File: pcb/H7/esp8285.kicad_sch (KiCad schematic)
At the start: 12 parts, among them U26 ESP8266EX

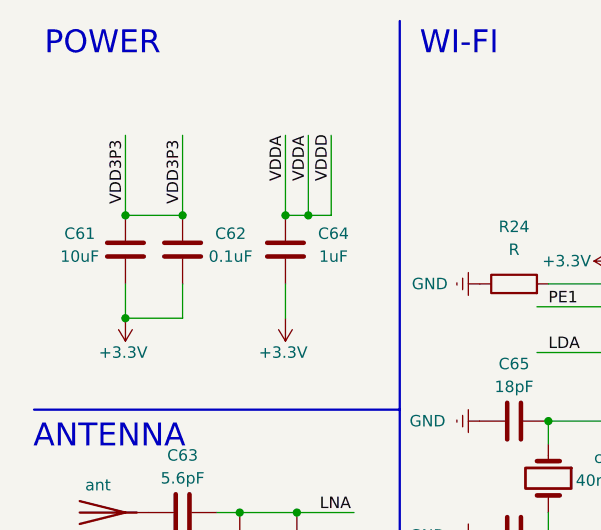
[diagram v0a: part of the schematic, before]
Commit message: schematic source updated
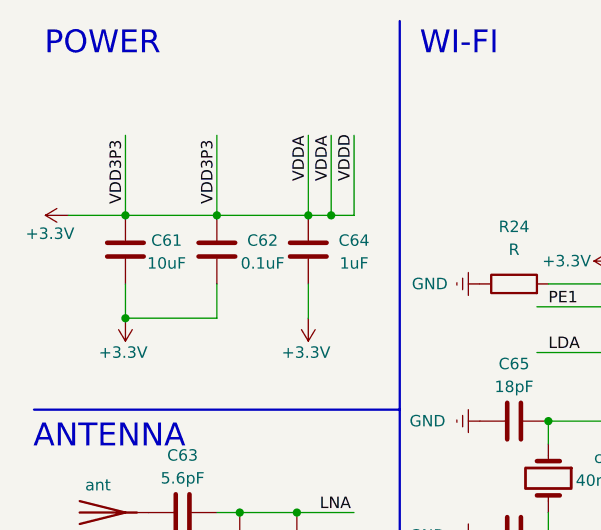
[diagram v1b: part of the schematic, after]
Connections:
- net VDD3P3 is gone; now on net +3.3V: C61.1, C62.2, U26.3 (VDD3P3), U26.4 (VDD3P3)
- net VDDA is gone; now on net +3.3V: C64.2, U26.1 (VDDA), U26.29 (VDDD), U26.30 (VDDA)
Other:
- moved on the sheet: C62, C64

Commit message: schematic fix
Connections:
- net +3.3V: no longer C61.2, C62.1, C64.1
- net GND: now also C61.2, C62.1, C64.1
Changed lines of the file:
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@@
+	)
+	(junction
+		(at 102.87 93.98)
+		(diameter 0)
+		(color 0 0 0 0)
 	)
 	(junction
@@
 	(junction
 		(at 115.57 115.57)
-		(diameter 0)
-		(color 0 0 0 0)
-	)
-	(junction
-		(at 102.87 93.98)
 		(diameter 0)
 		(color 0 0 0 0)
@@
 	(symbol
 		(lib_id "power:GNDREF")
+		(at 123.19 93.98 0)
+		(unit 1)
+		(exclude_from_sim no)
+		(in_bom yes)
+		(on_board yes)
+		(dnp no)
+		(property "Reference" "#PWR05"
+			(at 123.19 100.33 0)
+			(effects
+				(font
+					(size 1.27 1.27)
+				)
+				(hide yes)
+			)
+		)
+		(property "Value" "GND"
+			(at 124.968 98.044 0)
+			(effects
+				(font
+					(size 1.27 1.27)
+				)
+				(justify right)
+			)
+		)
+		(property "Footprint" ""
+			(at 123.19 93.98 0)
+			(effects
+				(font
+					(size 1.27 1.27)
+				)
+				(hide yes)
+			)
+		)
+		(property "Datasheet" ""
+			(at 123.19 93.98 0)
+			(effects
+				(font
+					(size 1.27 1.27)
+				)
+				(hide yes)
+			)
+		)
+		(property "Description" "Power symbol creates a global label with name \"GNDREF\" , reference supply ground"
+			(at 123.19 93.98 0)
+			(effects
+				(font
+					(size 1.27 1.27)
+				)
+				(hide yes)
+			)
+		)
+		(pin "1"
+		)
+		(instances
+			(project "project"
+				(path "/b61a0d2b-7633-4d0a-8bfd-ad16aaa1ff64/b2e80637-8828-4221-a6bd-d0ac0b787eac"
+					(reference "#PWR05")
+					(unit 1)
+				)
+			)
+		)
+	)
+	(symbol
+		(lib_id "power:GNDREF")
 		(at 115.57 123.19 0)
 		(unit 1)
@@
 	)
 	(symbol
-		(lib_id "power:+3.3V")
-		(at 102.87 93.98 180)
-		(unit 1)
-		(exclude_from_sim no)
-		(in_bom yes)
-		(on_board yes)
-		(dnp no)
-		(property "Reference" "#PWR0111"
-			(at 102.87 90.17 0)
-			(effects
-				(font
-					(size 1.27 1.27)
-				)
-				(hide yes)
-			)
-		)
-		(property "Value" "+3.3V"
-			(at 102.616 97.79 0)
-			(effects
-				(font
-					(size 1.27 1.27)
-				)
-			)
-		)
-		(property "Footprint" ""
-			(at 102.87 93.98 0)
-			(effects
-				(font
-					(size 1.27 1.27)
-				)
-				(hide yes)
-			)
-		)
-		(property "Datasheet" ""
-			(at 102.87 93.98 0)
-			(effects
-				(font
-					(size 1.27 1.27)
-				)
-				(hide yes)
-			)
-		)
-		(property "Description" "Power symbol creates a global label with name \"+3.3V\""
-			(at 102.87 93.98 0)
-			(effects
-				(font
-					(size 1.27 1.27)
-				)
-				(hide yes)
-			)
-		)
-		(pin "1"
-		)
-		(instances
-			(project "project"
-				(path "/b61a0d2b-7633-4d0a-8bfd-ad16aaa1ff64/b2e80637-8828-4221-a6bd-d0ac0b787eac"
-					(reference "#PWR0111")
-					(unit 1)
-				)
-			)
-		)
-	)
-	(symbol
-		(lib_id "power:+3.3V")
-		(at 123.19 93.98 180)
-		(unit 1)
-		(exclude_from_sim no)
-		(in_bom yes)
-		(on_board yes)
-		(dnp no)
-		(property "Reference" "#PWR0113"
-			(at 123.19 90.17 0)
-			(effects
-				(font
-					(size 1.27 1.27)
-				)
-				(hide yes)
-			)
-		)
-		(property "Value" "+3.3V"
-			(at 122.936 97.79 0)
-			(effects
-				(font
-					(size 1.27 1.27)
-				)
-			)
-		)
-		(property "Footprint" ""
-			(at 123.19 93.98 0)
-			(effects
-				(font
-					(size 1.27 1.27)
-				)
-				(hide yes)
-			)
-		)
-		(property "Datasheet" ""
-			(at 123.19 93.98 0)
-			(effects
-				(font
-					(size 1.27 1.27)
-				)
-				(hide yes)
-			)
-		)
-		(property "Description" "Power symbol creates a global label with name \"+3.3V\""
-			(at 123.19 93.98 0)
-			(effects
-				(font
-					(size 1.27 1.27)
-				)
-				(hide yes)
-			)
-		)
-		(pin "1"
-		)
-		(instances
-			(project "project"
-				(path "/b61a0d2b-7633-4d0a-8bfd-ad16aaa1ff64/b2e80637-8828-4221-a6bd-d0ac0b787eac"
-					(reference "#PWR0113")
-					(unit 1)
-				)
-			)
-		)
-	)
-	(symbol
 		(lib_id "Device:C")
 		(at 146.05 105.41 90)
@@
 					(unit 1)
 				)
+			)
+		)
+	)
+	(symbol
+		(lib_id "power:GNDREF")
+		(at 102.87 93.98 0)
+		(unit 1)
+		(exclude_from_sim no)
+		(in_bom yes)
+		(on_board yes)
+		(dnp no)
+		(property "Reference" "#PWR04"
+			(at 102.87 100.33 0)
+			(effects
+				(font
+					(size 1.27 1.27)
+				)
+				(hide yes)
+			)
+		)
+		(property "Value" "GND"
+			(at 104.648 98.044 0)
+			(effects
+				(font
+					(size 1.27 1.27)
+				)
+				(justify right)
+			)
+		)
+		(property "Footprint" ""
+			(at 102.87 93.98 0)
+			(effects
+				(font
+					(size 1.27 1.27)
+				)
+				(hide yes)
+			)
+		)
+		(property "Datasheet" ""
+			(at 102.87 93.98 0)
+			(effects
+				(font
+					(size 1.27 1.27)
+				)
+				(hide yes)
+			)
+		)
+		(property "Description" "Power symbol creates a global label with name \"GNDREF\" , reference supply ground"
+			(at 102.87 93.98 0)
+			(effects
+				(font
+					(size 1.27 1.27)
+				)
+				(hide yes)
+			)
+		)
+		(pin "1"
+		)
+		(instances
+			(project "project"
+				(path "/b61a0d2b-7633-4d0a-8bfd-ad16aaa1ff64/b2e80637-8828-4221-a6bd-d0ac0b787eac"
+					(reference "#PWR04")
+					(unit 1)
+				)

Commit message: trying to fix dshot issue with high frequency timer, schematic numbers fix
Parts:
- renumbered C61 to C19, C62 to C20, C64 to C28, C63 to C4, C65 to C5, C66 to C6, L5 to L1, L6 to L2, R24 to R12
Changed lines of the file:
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@@
 		(on_board yes)
 		(dnp no)
-		(property "Reference" "C62"
+		(property "Reference" "C20"
 			(at 118.11 85.344 0)
 			(effects
@@
 			(project "project"
 				(path "/b61a0d2b-7633-4d0a-8bfd-ad16aaa1ff64/b2e80637-8828-4221-a6bd-d0ac0b787eac"
-					(reference "C62")
+					(reference "C20")
 					(unit 1)
 				)
@@
 		(dnp no)
 		(fields_autoplaced yes)
-		(property "Reference" "R24"
+		(property "Reference" "R12"
 			(at 146.05 83.82 90)
 			(effects
@@
 			(project "project"
 				(path "/b61a0d2b-7633-4d0a-8bfd-ad16aaa1ff64/b2e80637-8828-4221-a6bd-d0ac0b787eac"
-					(reference "R24")
+					(reference "R12")
 					(unit 1)
 				)
@@
 		(on_board yes)
 		(dnp no)
-		(property "Reference" "L5"
+		(property "Reference" "L1"
 			(at 111.76 121.666 0)
 			(effects
@@
 			(project "project"
 				(path "/b61a0d2b-7633-4d0a-8bfd-ad16aaa1ff64/b2e80637-8828-4221-a6bd-d0ac0b787eac"
-					(reference "L5")
+					(reference "L1")
 					(unit 1)
 				)
@@
 		(on_board yes)
 		(dnp no)
-		(property "Reference" "C63"
+		(property "Reference" "C4"
 			(at 109.22 109.22 90)
 			(effects
@@
 			(project "project"
 				(path "/b61a0d2b-7633-4d0a-8bfd-ad16aaa1ff64/b2e80637-8828-4221-a6bd-d0ac0b787eac"
-					(reference "C63")
+					(reference "C4")
 					(unit 1)
 				)
@@
 		(on_board yes)
 		(dnp no)
-		(property "Reference" "C64"
+		(property "Reference" "C28"
 			(at 128.27 85.344 0)
 			(effects
@@
 			(project "project"
 				(path "/b61a0d2b-7633-4d0a-8bfd-ad16aaa1ff64/b2e80637-8828-4221-a6bd-d0ac0b787eac"
-					(reference "C64")
+					(reference "C28")
 					(unit 1)
 				)
@@
 		(on_board yes)
 		(dnp no)
-		(property "Reference" "L6"
+		(property "Reference" "L2"
 			(at 125.984 121.666 0)
 			(effects
@@
 			(project "project"
 				(path "/b61a0d2b-7633-4d0a-8bfd-ad16aaa1ff64/b2e80637-8828-4221-a6bd-d0ac0b787eac"
-					(reference "L6")
+					(reference "L2")
 					(unit 1)
 				)
@@
 		(on_board yes)
 		(dnp no)
-		(property "Reference" "C66"
+		(property "Reference" "C6"
 			(at 145.796 122.174 90)
 			(effects
@@
 			(project "project"
 				(path "/b61a0d2b-7633-4d0a-8bfd-ad16aaa1ff64/b2e80637-8828-4221-a6bd-d0ac0b787eac"
-					(reference "C66")
+					(reference "C6")
 					(unit 1)
 				)
@@
 		(on_board yes)
 		(dnp no)
-		(property "Reference" "C65"
+		(property "Reference" "C5"
 			(at 146.05 99.06 90)
 			(effects
@@
 			(project "project"
 				(path "/b61a0d2b-7633-4d0a-8bfd-ad16aaa1ff64/b2e80637-8828-4221-a6bd-d0ac0b787eac"
-					(reference "C65")
+					(reference "C5")
 					(unit 1)
 				)
@@
 		(on_board yes)
 		(dnp no)
-		(property "Reference" "C61"
+		(property "Reference" "C19"
 			(at 107.442 85.344 0)
 			(effects
@@
 			(project "project"
 				(path "/b61a0d2b-7633-4d0a-8bfd-ad16aaa1ff64/b2e80637-8828-4221-a6bd-d0ac0b787eac"
-					(reference "C61")
-					(unit 1)
-				)
+					(reference "C19")
+					(unit 1)
+				)

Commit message: esp8266 spi fix
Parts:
- renumbered cr4 to cr2
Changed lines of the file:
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@@
 		(on_board yes)
 		(dnp no)
-		(property "Reference" "cr4"
+		(property "Reference" "cr2"
 			(at 154.94 109.474 90)
 			(effects
@@
 			(project "project"
 				(path "/b61a0d2b-7633-4d0a-8bfd-ad16aaa1ff64/b2e80637-8828-4221-a6bd-d0ac0b787eac"
-					(reference "cr4")
+					(reference "cr2")
 					(unit 1)
 				)
